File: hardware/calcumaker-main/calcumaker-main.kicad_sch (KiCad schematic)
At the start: 0 parts

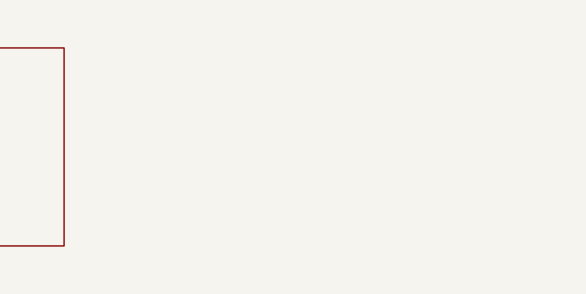
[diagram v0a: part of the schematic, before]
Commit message: Hardware: annunciator LED sheet on the main board (f g C G low-batt)
New 7th subsheet 'Annunciators' in the calcumaker-main manifest: D61-D65 +
R9-R13 (470R 0402 C25117), MCU GPIO direct — f yellow (Everlight C72038) and
g blue (C965807) beside the shift keys, C/G/low-batt red (KT-0603R C2286)
along the top edge under the display bezel. Board regenerates + passes the
structure check (159 comp, 159/159 footprints, no dup refs). PARTS.md, pin
budget (+5 GPIO), sheet plan, and Open Q6 (now decided) updated.

Co-Authored-By: Claude Fable 5 <noreply@anthropic.com>
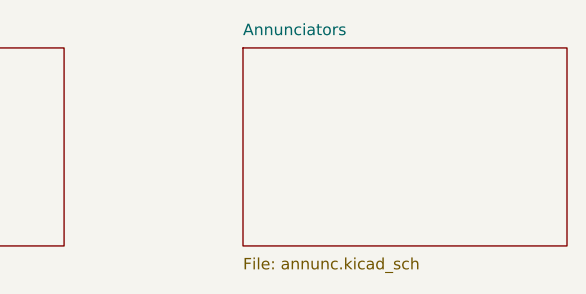
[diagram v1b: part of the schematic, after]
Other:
- added sheet Annunciators (annunc.kicad_sch)
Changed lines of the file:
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@@
+		)
+	)
+	(sheet
+		(at 375.92 40.64)
+		(size 36.00 22.00)
+		(fields_autoplaced yes)
+		(stroke (width 0.1524) (type solid))
+		(fill (color 0 0 0 0.0000))
+		(property "Sheetname" "Annunciators"
+			(at 375.92 39.37 0)
+			(effects (font (size 1.27 1.27)) (justify left bottom))
+		)
+		(property "Sheetfile" "annunc.kicad_sch"
+			(at 375.92 63.91 0)
+			(effects (font (size 1.27 1.27)) (justify left top))
 		)
 	)
